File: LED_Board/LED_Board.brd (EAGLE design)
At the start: 99.1 x 96.5 mm, 16 parts

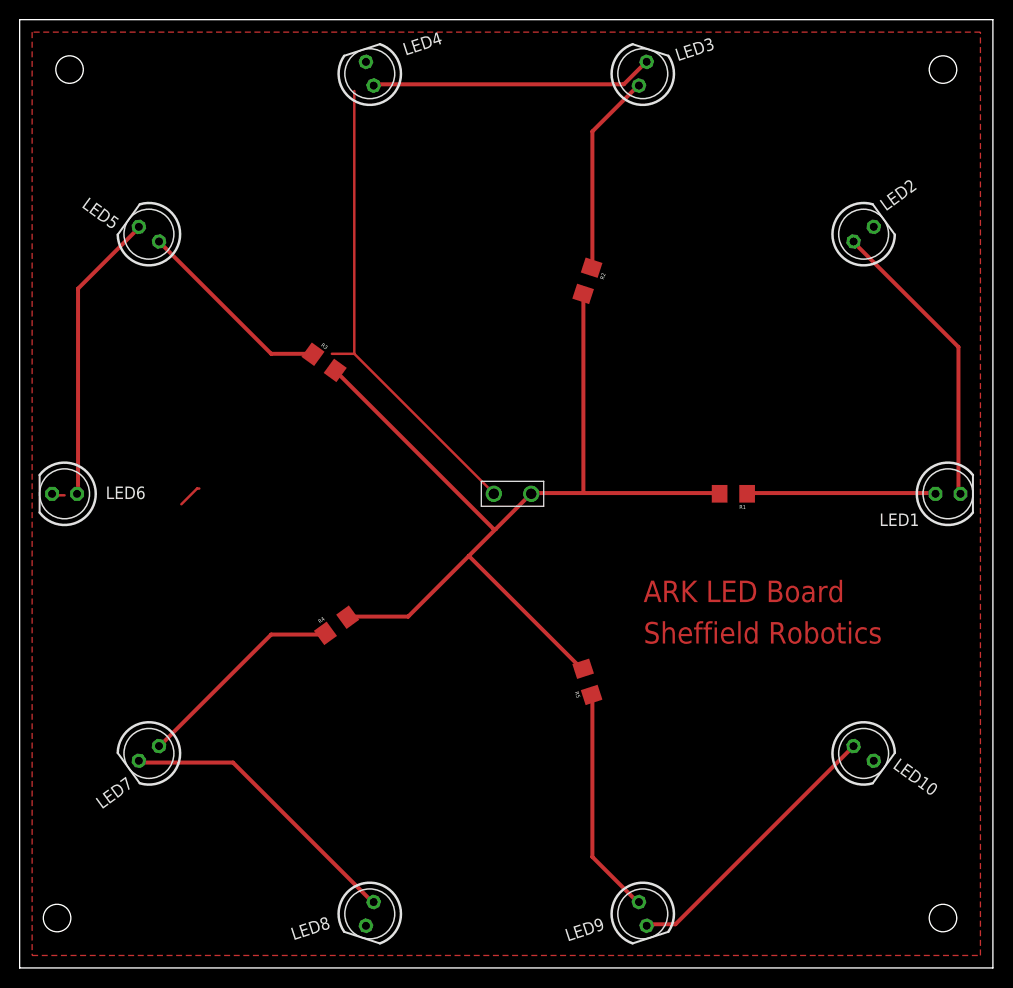
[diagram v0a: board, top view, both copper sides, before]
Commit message: * Added LED to the control board for indicating that the OHC is sending a command * Corrections on the silkscreen for both boards (size of the names of the components)
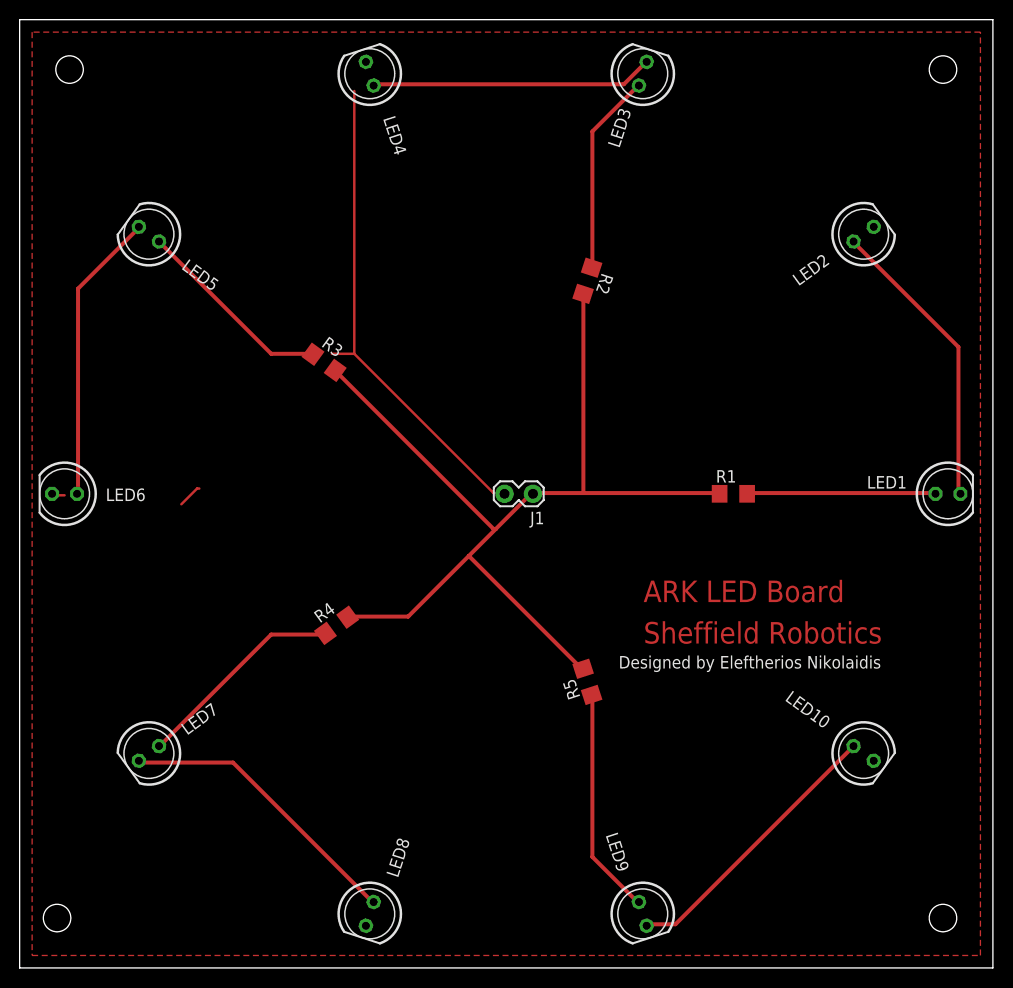
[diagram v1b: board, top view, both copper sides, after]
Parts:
- J1: value (none) -> +; device Connectors:1X02_BIG -> Connectors:1X02_LOCK
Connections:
- net GND: now also J1.2; no longer J1.P$2
- net N$1: now also J1.1; no longer J1.P$1
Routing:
- net GND: track 53.2 -> 54.3 mm
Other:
- board text added: "Designed by Eleftherios Nikolaidis"
